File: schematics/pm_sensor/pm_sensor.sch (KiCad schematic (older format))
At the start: 20 parts, among them J1 sds011_conn, J2 Conn_01x03, J3 conn_display, Q1 2N7000TA, Q2 2N7000TA, Q3 2N7000TA, Q4 IRF9510, U1 WeMos_D1_mini, U2 DHT22

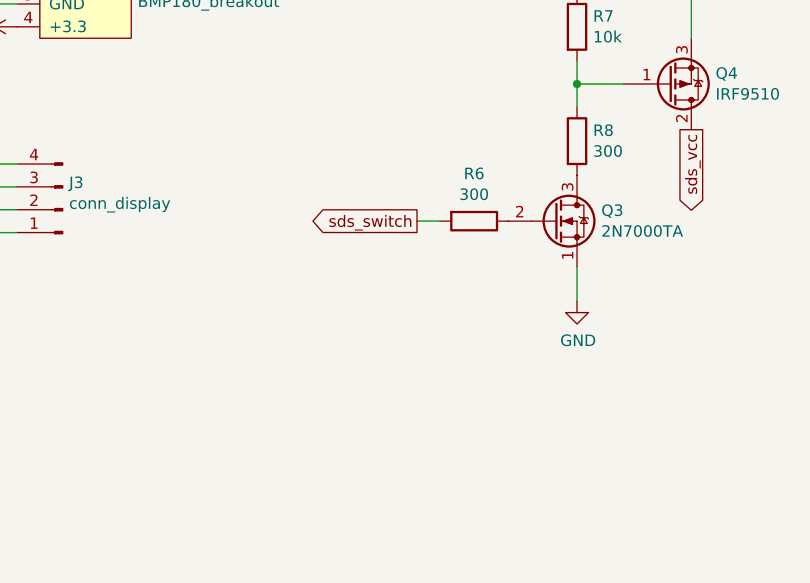
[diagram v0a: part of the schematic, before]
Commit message: Add pulldown on SDS011 switch pin
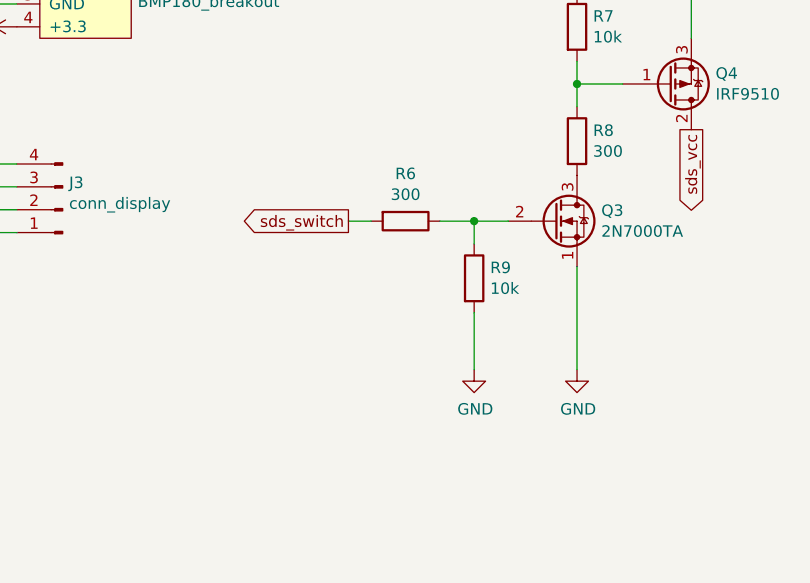
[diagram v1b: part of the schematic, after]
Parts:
- added R9: 10k, Resistor_THT:R_Axial_DIN0207_L6.3mm_D2.5mm_P10.16mm_Horizontal, symbol Device:R
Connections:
- net GND: now also R9.2
- net at Q3.2 (G), R6.1: now also R9.1
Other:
- moved on the sheet: R6
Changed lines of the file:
@@
 L power:GND #PWR0102
 U 1 1 5CDF1575
-P 8850 2400
-F 0 "#PWR0102" H 8850 2150 50  0001 C CNN
-F 1 "GND" H 8855 2227 50  0000 C CNN
-F 2 "" H 8850 2400 50  0001 C CNN
-F 3 "" H 8850 2400 50  0001 C CNN
-F 4 "I" H 8850 2400 50  0001 C CNN "Spice_Primitive"
-F 5 "dc 0" H 8850 2400 50  0001 C CNN "Spice_Model"
-F 6 "Y" H 8850 2400 50  0001 C CNN "Spice_Netlist_Enabled"
-	1    8850 2400
+P 8850 2700
+F 0 "#PWR0102" H 8850 2450 50  0001 C CNN
+F 1 "GND" H 8855 2527 50  0000 C CNN
+F 2 "" H 8850 2700 50  0001 C CNN
+F 3 "" H 8850 2700 50  0001 C CNN
+F 4 "I" H 8850 2700 50  0001 C CNN "Spice_Primitive"
+F 5 "dc 0" H 8850 2700 50  0001 C CNN "Spice_Model"
+F 6 "Y" H 8850 2700 50  0001 C CNN "Spice_Netlist_Enabled"
+	1    8850 2700
 	1    0    0    -1
 $EndComp
@@
 L Device:R R6
 U 1 1 5CE2396C
-P 8400 2050
-F 0 "R6" V 8193 2050 50  0000 C CNN
-F 1 "300" V 8284 2050 50  0000 C CNN
-F 2 "Resistor_THT:R_Axial_DIN0207_L6.3mm_D2.5mm_P10.16mm_Horizontal" V 8330 2050 50  0001 C CNN
-F 3 "~" H 8400 2050 50  0001 C CNN
-	1    8400 2050
+P 8100 2050
+F 0 "R6" V 7893 2050 50  0000 C CNN
+F 1 "300" V 7984 2050 50  0000 C CNN
+F 2 "Resistor_THT:R_Axial_DIN0207_L6.3mm_D2.5mm_P10.16mm_Horizontal" V 8030 2050 50  0001 C CNN
+F 3 "~" H 8100 2050 50  0001 C CNN
+	1    8100 2050
 	0    1    1    0
 $EndComp
@@
 	8650 950  8850 950
 Connection ~ 8850 950
-Wire Wire Line
-	8850 2250 8850 2400
-Text GLabel 8150 2050 0    50   Output ~ 0
+Text GLabel 7850 2050 0    50   Output ~ 0
 sds_switch
 Text GLabel 9350 1650 3    50   Output ~ 0
@@
 sds_vcc
 Wire Wire Line
-	8150 2050 8250 2050
+	7850 2050 7950 2050
 Text GLabel 2900 2250 2    50   Output ~ 0
 sds_switch
@@
 	4350 2300 4500 2300
 $Comp
-L power:GND #PWR?
+L power:GND #PWR0120
 U 1 1 5CE71516
 P 4500 2600
-F 0 "#PWR?" H 4500 2350 50  0001 C CNN
+F 0 "#PWR0120" H 4500 2350 50  0001 C CNN
 F 1 "GND" H 4505 2427 50  0000 C CNN
 F 2 "" H 4500 2600 50  0001 C CNN
@@
 	1    0    0    -1
 $EndComp
+$Comp
+L power:GND #PWR01
+U 1 1 5CEA2330
+P 8400 2700
+F 0 "#PWR01" H 8400 2450 50  0001 C CNN
+F 1 "GND" H 8405 2527 50  0000 C CNN
+F 2 "" H 8400 2700 50  0001 C CNN
+F 3 "" H 8400 2700 50  0001 C CNN
+F 4 "I" H 8400 2700 50  0001 C CNN "Spice_Primitive"
+F 5 "dc 0" H 8400 2700 50  0001 C CNN "Spice_Model"
+F 6 "Y" H 8400 2700 50  0001 C CNN "Spice_Netlist_Enabled"
+	1    8400 2700
+	1    0    0    -1
+$EndComp
+$Comp
+L Device:R R9
+U 1 1 5CEA2ED1
+P 8400 2300
+F 0 "R9" H 8470 2346 50  0000 L CNN
+F 1 "10k" H 8470 2255 50  0000 L CNN
+F 2 "Resistor_THT:R_Axial_DIN0207_L6.3mm_D2.5mm_P10.16mm_Horizontal" V 8330 2300 50  0001 C CNN
+F 3 "~" H 8400 2300 50  0001 C CNN
+	1    8400 2300
+	1    0    0    -1
+$EndComp
+Wire Wire Line
+	8850 2250 8850 2700
+Wire Wire Line
+	8250 2050 8400 2050
+Wire Wire Line
+	8400 2150 8400 2050
+Connection ~ 8400 2050
+Wire Wire Line
+	8400 2050 8550 2050
+Wire Wire Line
+	8400 2450 8400 2700
 $EndSCHEMATC

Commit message: Some schematic changes (dunno)
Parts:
- removed C1: 100nF, Capacitor_THT:C_Disc_D5.0mm_W2.5mm_P5.00mm, symbol Device:C
- removed J2: Conn_01x03, symbol Connector_Generic:Conn_01x03
- removed J3: conn_display, Connector_PinHeader_2.54mm:PinHeader_1x04_P2.54mm_Vertical, symbol Connector:Conn_01x04_Male
- removed Q1, Q2: 2N7000TA, Package_TO_SOT_THT:TO-92_Inline_Wide, symbol Transistor_FET:2N7000
- removed R2, R3, R4, R5: 10k, Resistor_THT:R_Axial_DIN0207_L6.3mm_D2.5mm_P10.16mm_Horizontal, symbol Device:R
- added J3: display_conn, Connector_PinHeader_2.54mm:PinHeader_1x08_P2.54mm_Vertical, symbol Connector:Conn_01x08_Male
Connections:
- net +3V3: now also J3.6 (Pin_6)
- net GND: now also J3.2 (Pin_2), J3.8 (Pin_8)
- net rst: now reaches U1.1 (~RST)
- net rst: now also J3.1 (Pin_1)
- net display_din: now reaches U1.11 (D4)
- net display_din: now also J3.4 (Pin_4)
- net display_dc: now reaches U1.12 (D3)
- net display_dc: now also J3.3 (Pin_3)
- net display_clk: now reaches U1.7 (CS/D8)
- net display_clk: now also J3.5 (Pin_5)
- no-connect marks 8 -> 4
